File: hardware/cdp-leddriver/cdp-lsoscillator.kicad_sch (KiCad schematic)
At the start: 8 parts, among them U8 74LS132, U9 74LS74

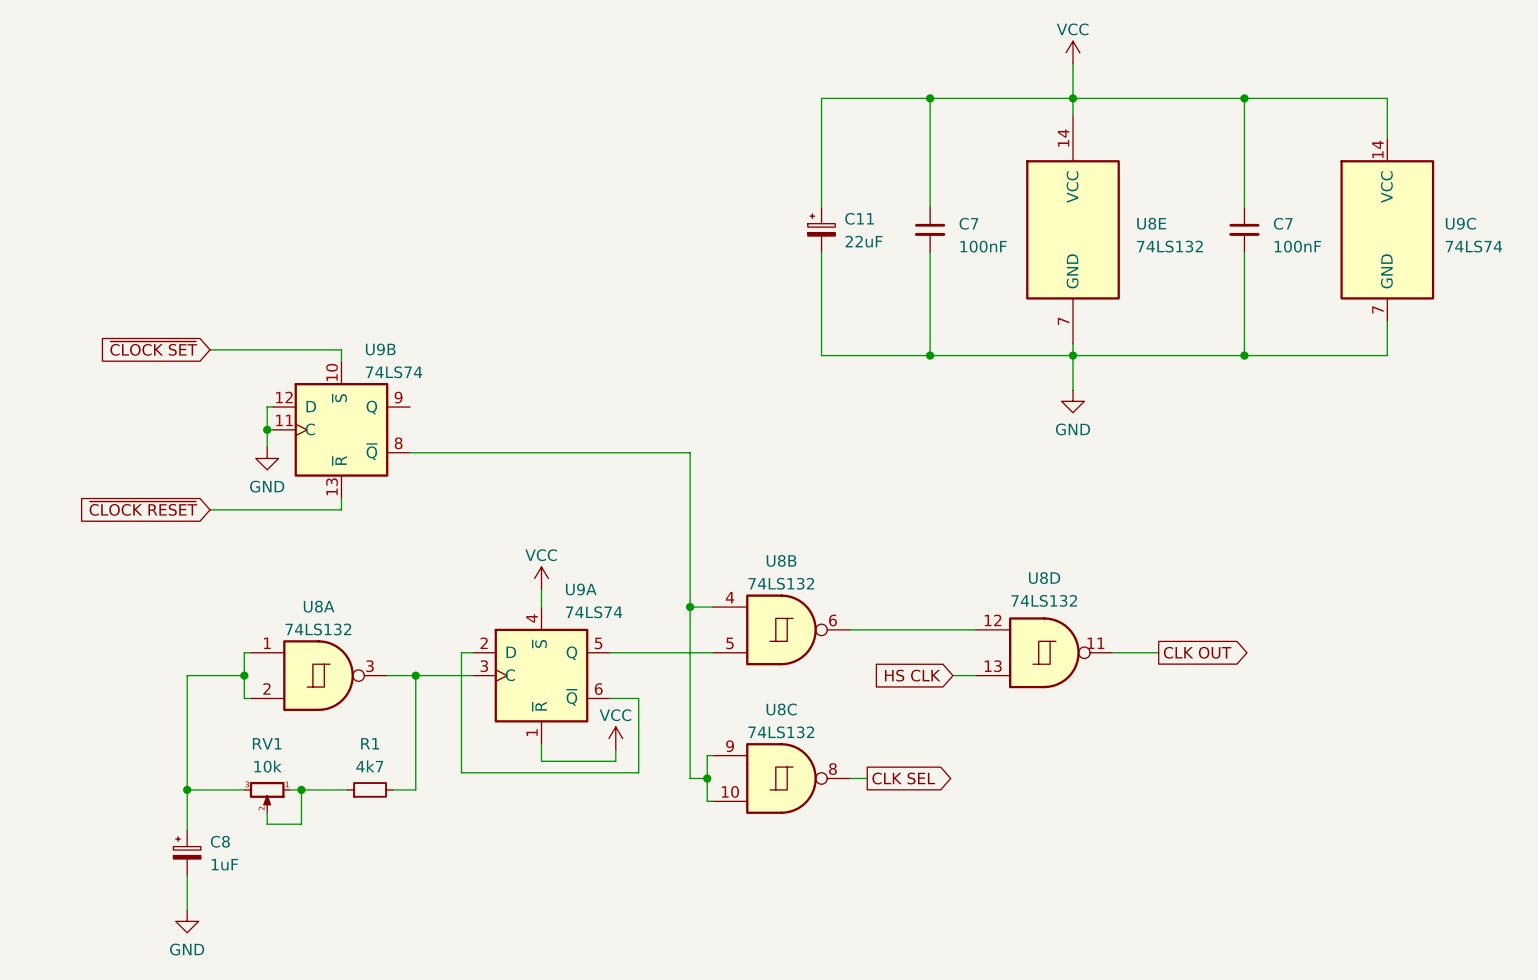
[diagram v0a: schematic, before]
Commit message: IC names fixed on the led driver schematic, on the PCB the MA8-MA15 labels were misaligned that is also fixed. Updated the gerber files.
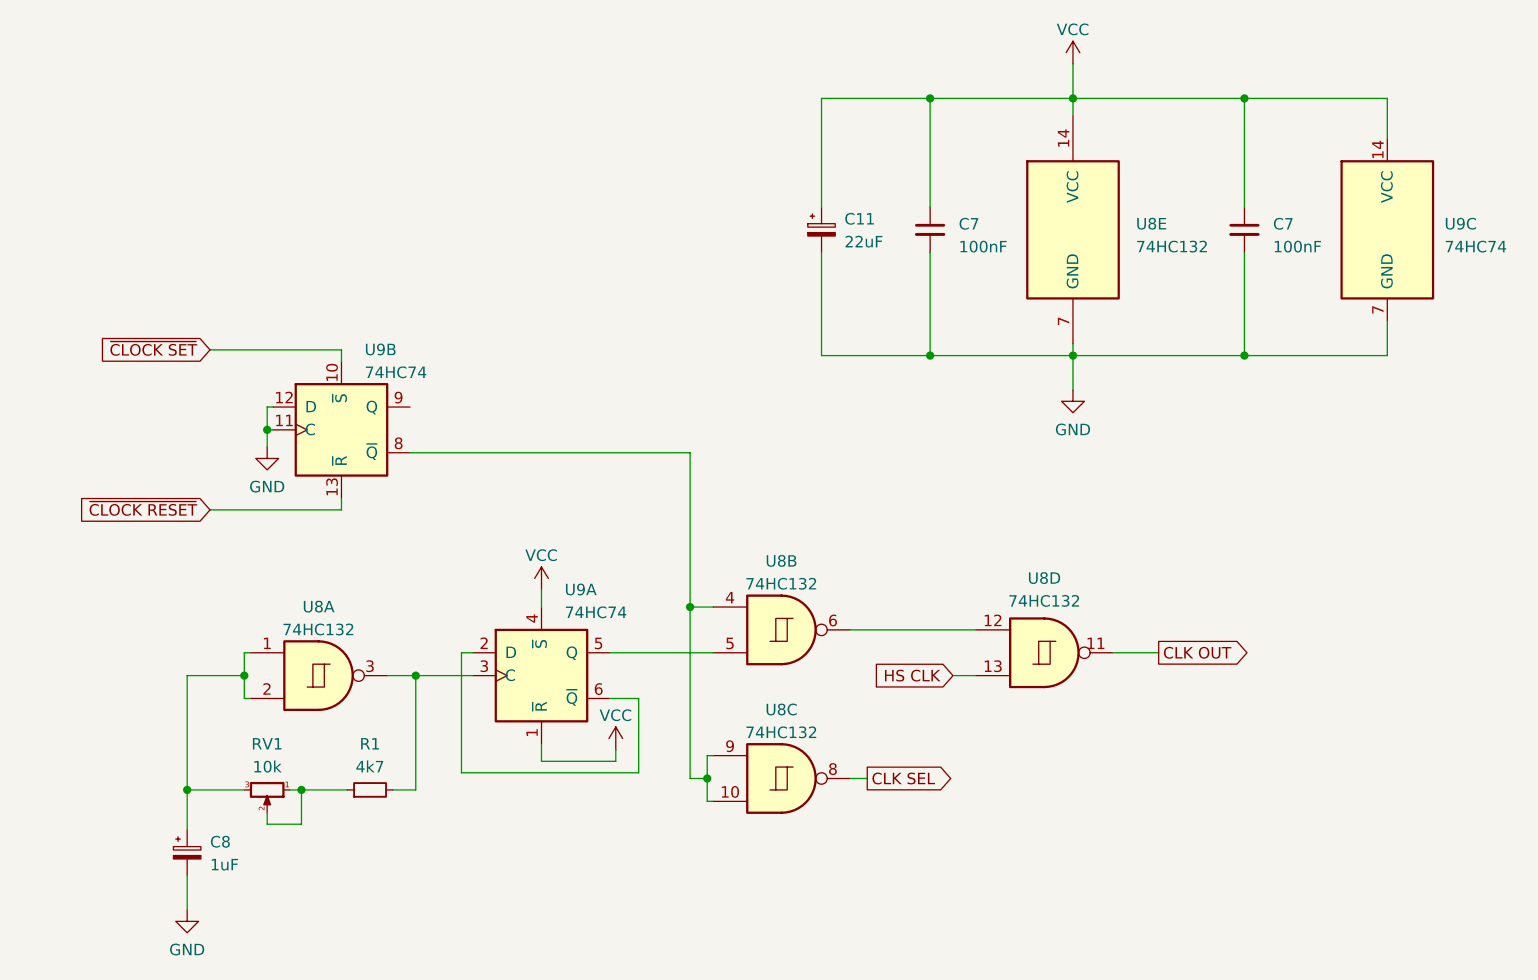
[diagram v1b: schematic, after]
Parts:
- U8: value 74LS132 -> 74HC132
- U9: value 74LS74 -> 74HC74
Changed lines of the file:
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@@
       (effects (font (size 1.27 1.27)))
     )
-    (property "Value" "74LS132" (at 137.1517 85.725 0)
+    (property "Value" "74HC132" (at 137.1517 85.725 0)
       (effects (font (size 1.27 1.27)))
     )
@@
       (effects (font (size 1.27 1.27)) (justify left))
     )
-    (property "Value" "74LS132" (at 176.53 48.26 0)
+    (property "Value" "74HC132" (at 176.53 48.26 0)
       (effects (font (size 1.27 1.27)) (justify left))
     )
@@
       (effects (font (size 1.27 1.27)) (justify left))
     )
-    (property "Value" "74LS74" (at 210.82 48.26 0)
+    (property "Value" "74HC74" (at 210.82 48.26 0)
       (effects (font (size 1.27 1.27)) (justify left))
     )
@@
       (effects (font (size 1.27 1.27)) (justify left))
     )
-    (property "Value" "74LS74" (at 90.8305 62.23 0)
+    (property "Value" "74HC74" (at 90.8305 62.23 0)
       (effects (font (size 1.27 1.27)) (justify left))
     )
@@
       (effects (font (size 1.27 1.27)))
     )
-    (property "Value" "74LS132" (at 85.7167 90.805 0)
+    (property "Value" "74HC132" (at 85.7167 90.805 0)
       (effects (font (size 1.27 1.27)))
     )
@@
       (effects (font (size 1.27 1.27)) (justify left))
     )
-    (property "Value" "74LS74" (at 113.0555 88.9 0)
+    (property "Value" "74HC74" (at 113.0555 88.9 0)
       (effects (font (size 1.27 1.27)) (justify left))
     )
@@
       (effects (font (size 1.27 1.27)))
     )
-    (property "Value" "74LS132" (at 137.1517 102.235 0)
+    (property "Value" "74HC132" (at 137.1517 102.235 0)
       (effects (font (size 1.27 1.27)))
     )
@@
       (effects (font (size 1.27 1.27)))
     )
-    (property "Value" "74LS132" (at 166.3617 87.63 0)
-      (effects (font (size 1.27 1.27)))
-    )
+    (property "Value" "74HC132" (at 166.3617 87.63 0)
+      (effects (font (size 1.27 1.27)))
+    )
